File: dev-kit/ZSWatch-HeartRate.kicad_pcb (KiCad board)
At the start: 4 copper layers, 45 x 36.9 mm, 49 parts, among them IC101 LIS2DS12, IC102 MCP73832-2-OT, IC103 MAX32664, IC104 TPS61240, IC105 MAX86141, IC106 MIC5365-1.8, J101 SPI, J104 I2C, M101 BM15C, Q101 BSS138, SW101 BTN1, SW102 RESET, X102 CHARGE, X103 BATTERY, X104 DEBUG, Y101 32kHz

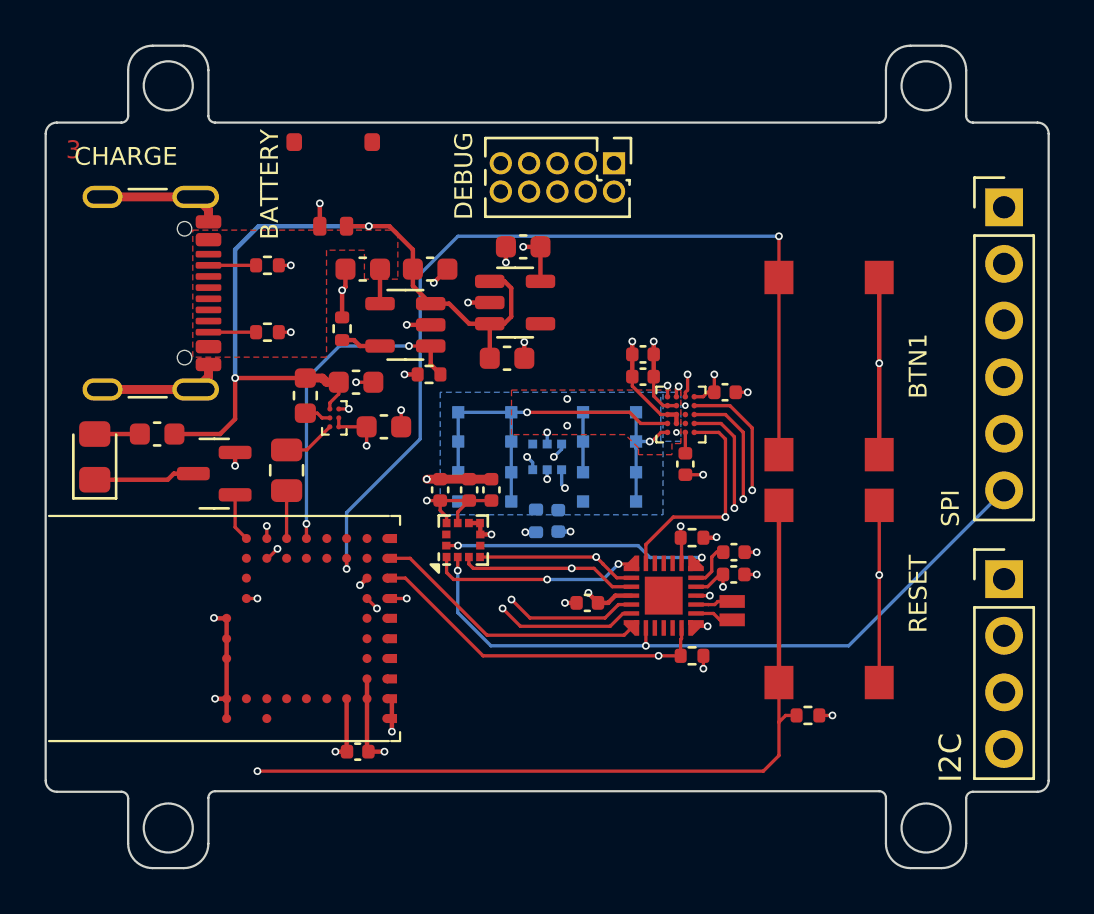
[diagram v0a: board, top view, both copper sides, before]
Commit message: Feature: Issue #16
- Add MFIO to SPI header

Signed-off-by: Daniel Kampert <DanielKampert@kampis-elektroecke.de>
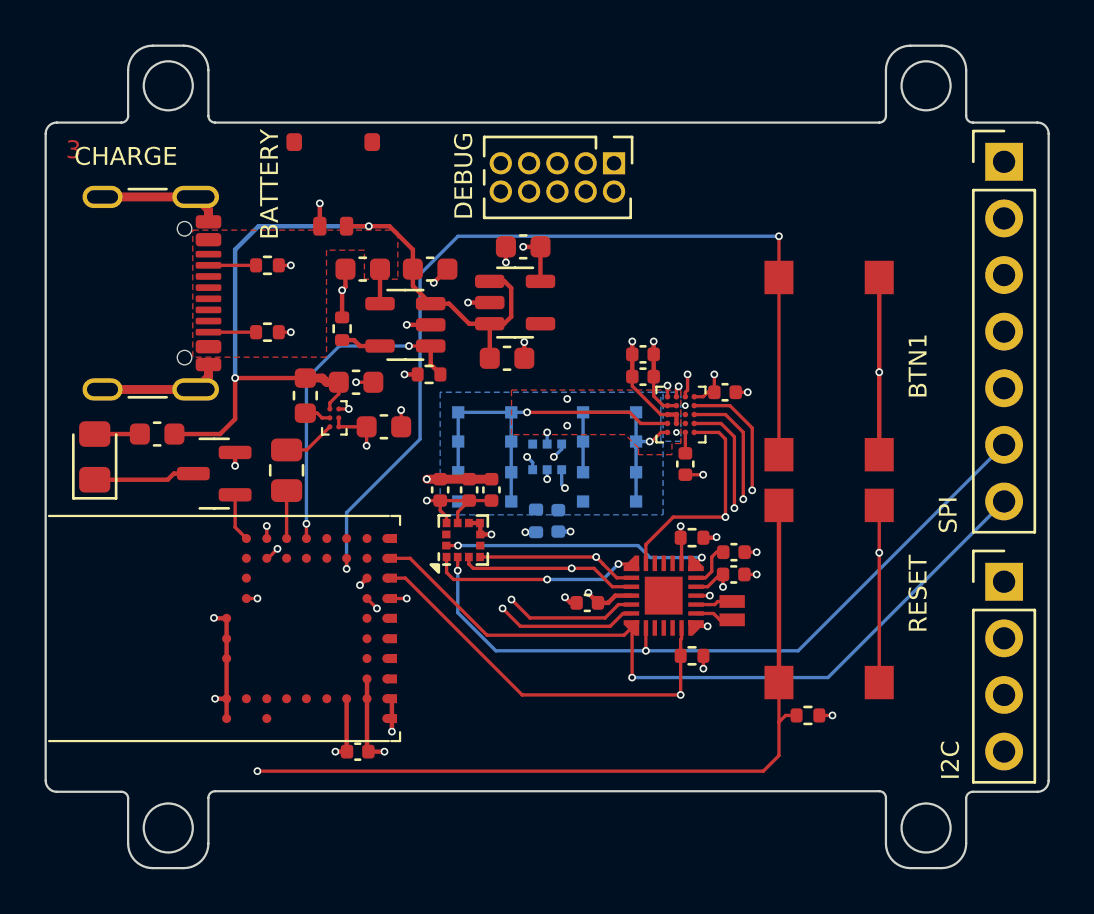
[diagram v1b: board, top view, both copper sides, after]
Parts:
- J101: footprint Connector_PinHeader_2.54mm:PinHeader_1x06_P2.54mm_Vertical -> Connector_PinHeader_2.54mm:PinHeader_1x07_P2.54mm_Vertical
- moved J101 2.04 mm to (184.2, 89.5)
- moved J104 0.11 mm to (184.2, 108.3)
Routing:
- net /STATUS: track 12.4 -> 34.6 mm, vias 0 -> 1
- net Net-(IC101-SCL/SCLK): track 41.6 -> 43.0 mm
- net Net-(IC101-CS): track 31.3 -> 32.6 mm
- net Net-(IC101-SDA/SDI/SDO): track 34.1 -> 34.9 mm
- net Net-(IC103-CS_{PPG}): track 24.0 -> 24.8 mm
- net Net-(IC101-SDO/ADDR0): track 37.6 -> 38.4 mm
- net /~{RESET_{HR}}: track 31.8 -> 32.7 mm
